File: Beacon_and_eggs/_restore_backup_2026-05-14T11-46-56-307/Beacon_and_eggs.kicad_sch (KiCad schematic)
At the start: 71 parts, among them J1 USB_C_Receptacle_USB2.0_16P, J2 Conn_01x03_Pin, J3 Conn_01x02_Pin, Q1 NTA4151P, Q2 NTA4153N, SW3 RESET, SW4 BOOT0, U1 SA868S, U2 STM32F411CEU6TR, U3 ADXL343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

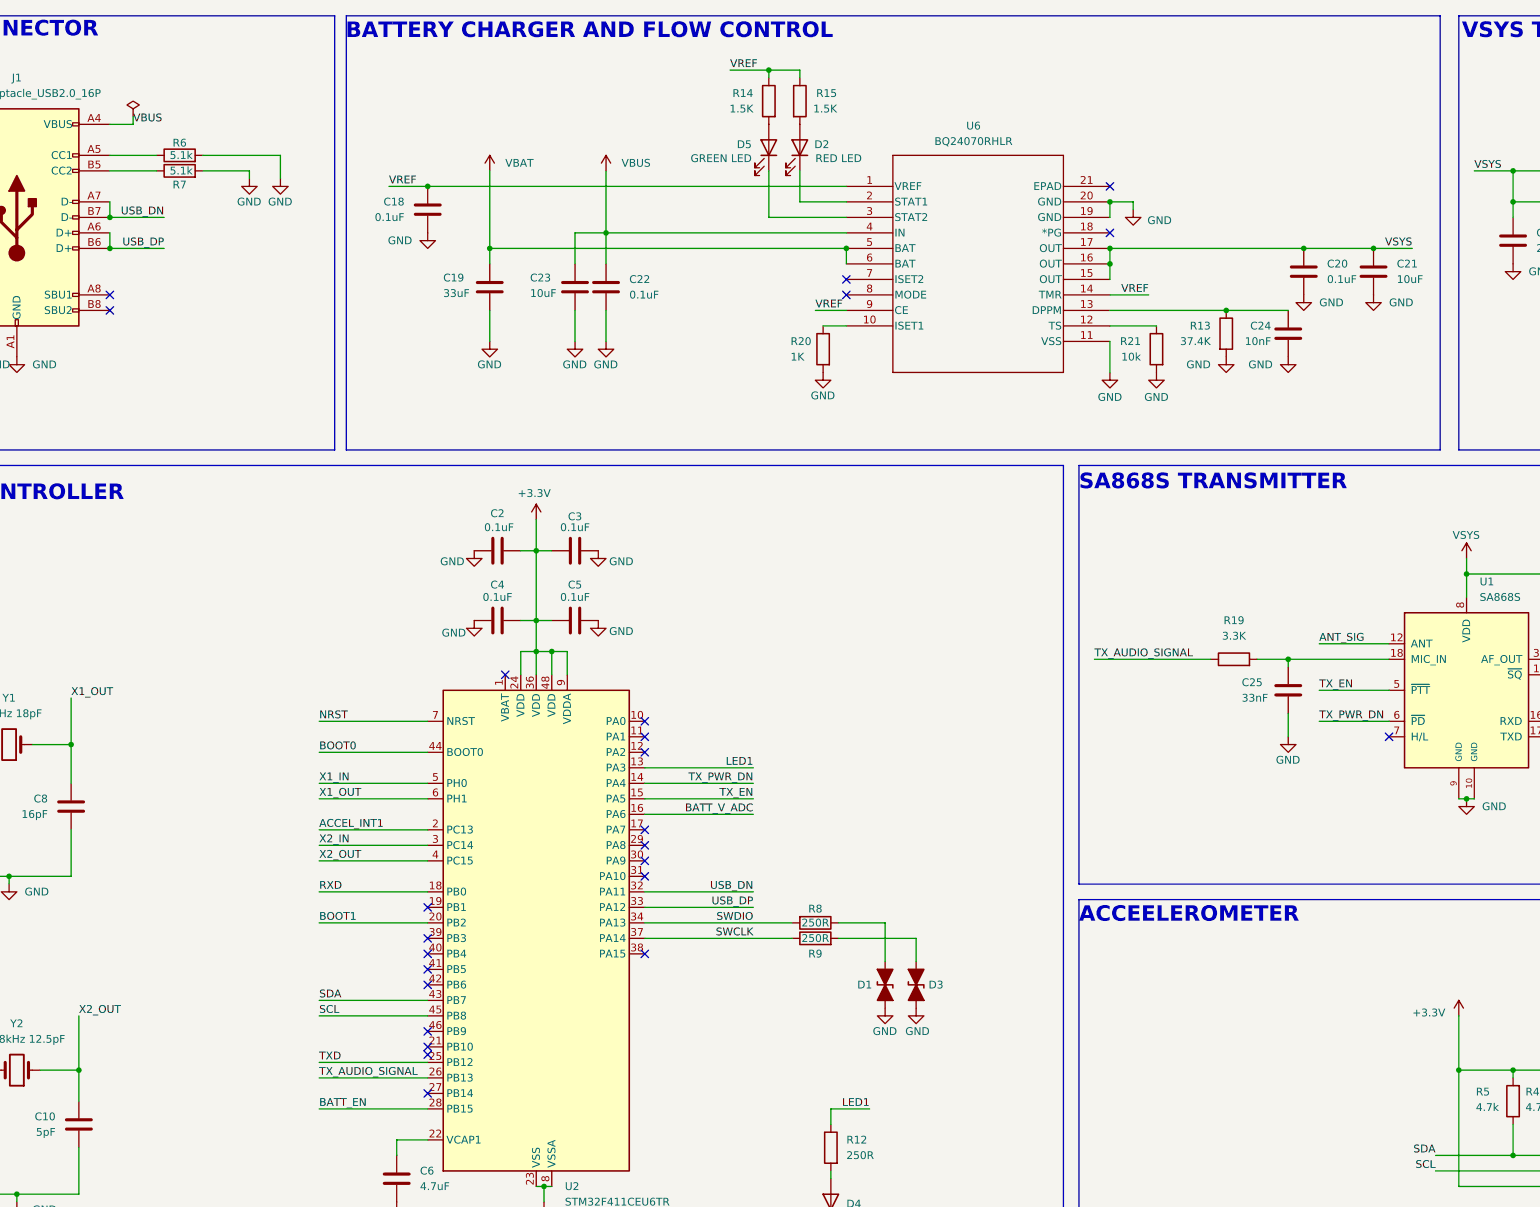
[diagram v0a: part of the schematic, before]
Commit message: fixed accel. pinouts, added 10k resistor to TS of U6
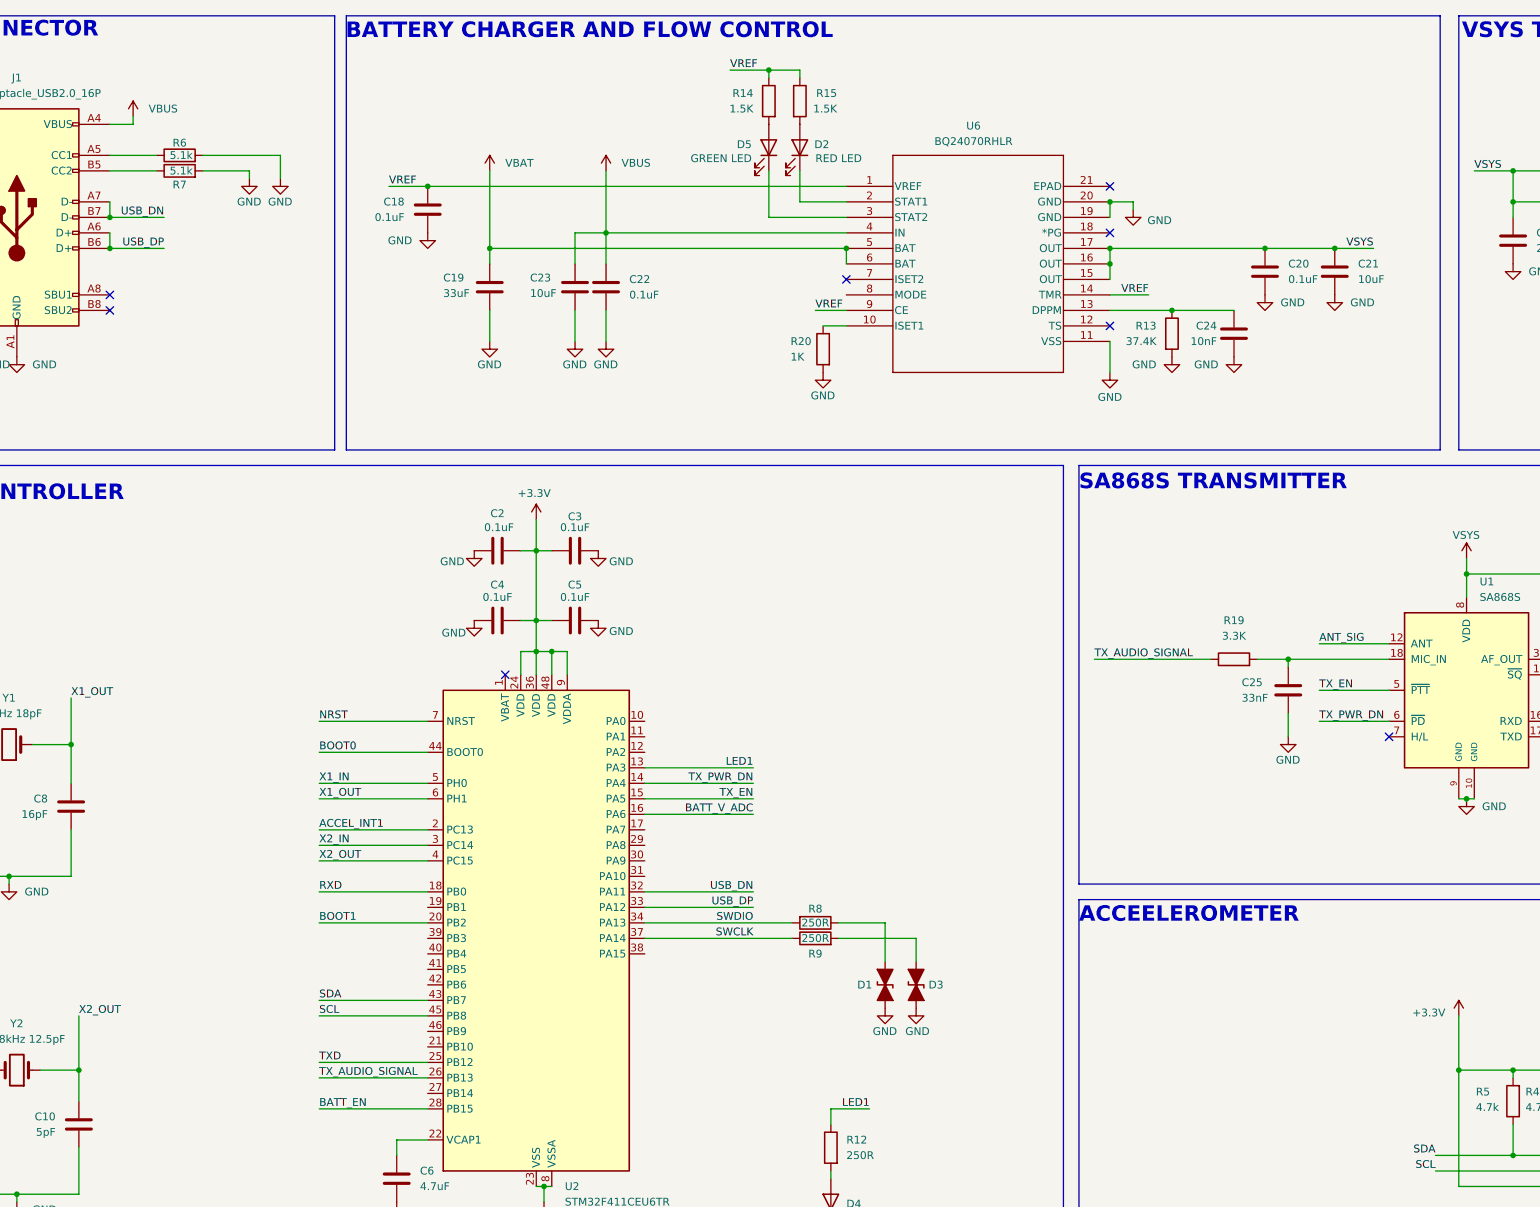
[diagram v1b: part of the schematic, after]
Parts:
- removed R21: 10k, Resistor_SMD:R_0402_1005Metric_Pad0.72x0.64mm_HandSolder, symbol Device:R
- 3V3: MANUFACTURER C0402C104K4RACTU -> (none); Manufacturer (none) -> C0402C104K4RACTU
- D4: Manufacturer (none) -> Lite-On Inc.
- R12: Manufacturer (none) -> YAGEO
- U6: PACKAGE VQFN-20 Texas Instruments -> (none); Package (none) -> VQFN-20 Texas Instruments
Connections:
- no-connect marks 30 -> 13
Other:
- moved on the sheet: C20, C21, C24, R13
